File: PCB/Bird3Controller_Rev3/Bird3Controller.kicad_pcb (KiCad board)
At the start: 2 copper layers, 43 x 108 mm, 61 parts, among them IC1 M24C08-RMN6TP, IC2 AP63203WU-7, J1 Bird 3 24-pin Connector, J2 TXW154028S0 Connector, J3 87832-2220, J4 Adafruit USB-C Breakout, Q1 2N7002A, SW1 SW_Boot, SW2 SW_Reset, U1 ESP32-S3-WROOM-1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

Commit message: Switch to thermal reliefs for pad connections except for thermal pads. Also move some traces around to optimize the thermal reliefs
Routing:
- net GND: track 379.3 -> 383.5 mm, vias 145 -> 151

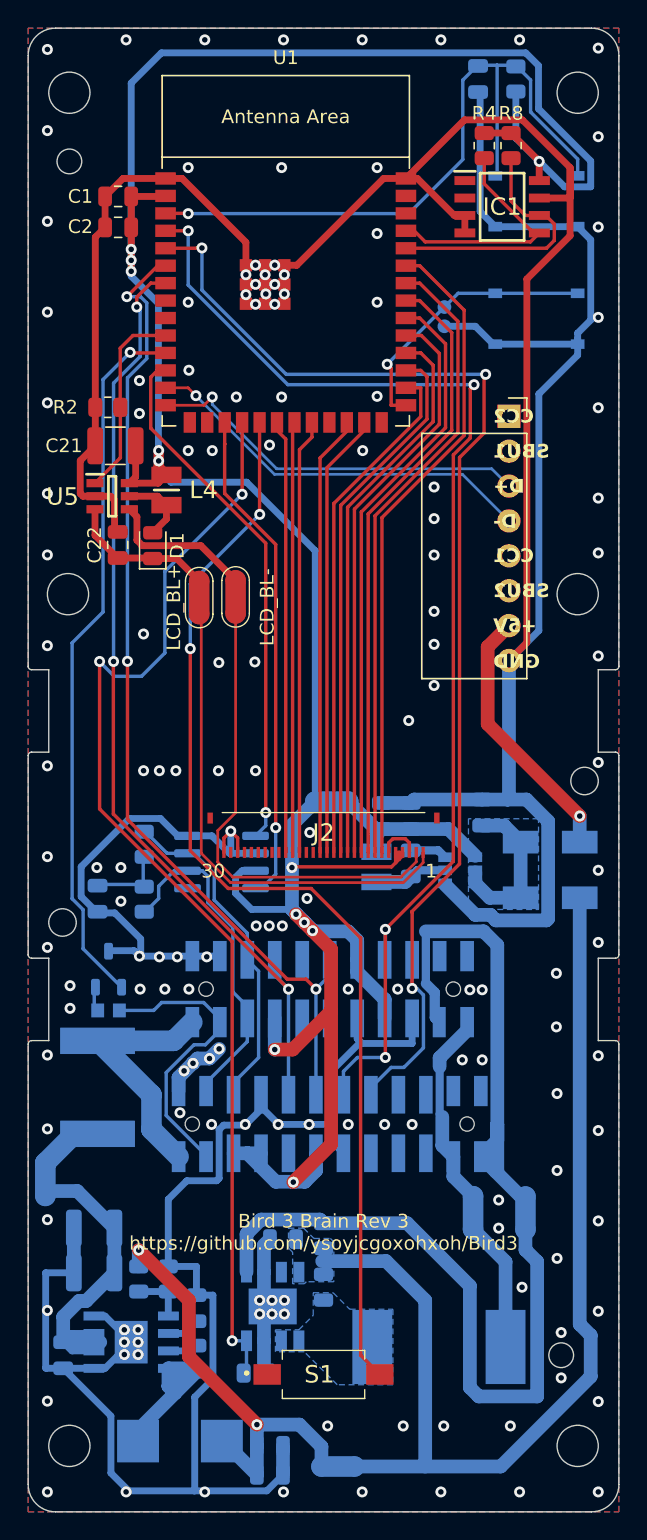
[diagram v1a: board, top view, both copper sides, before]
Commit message: Rearrange and add ground plane vias
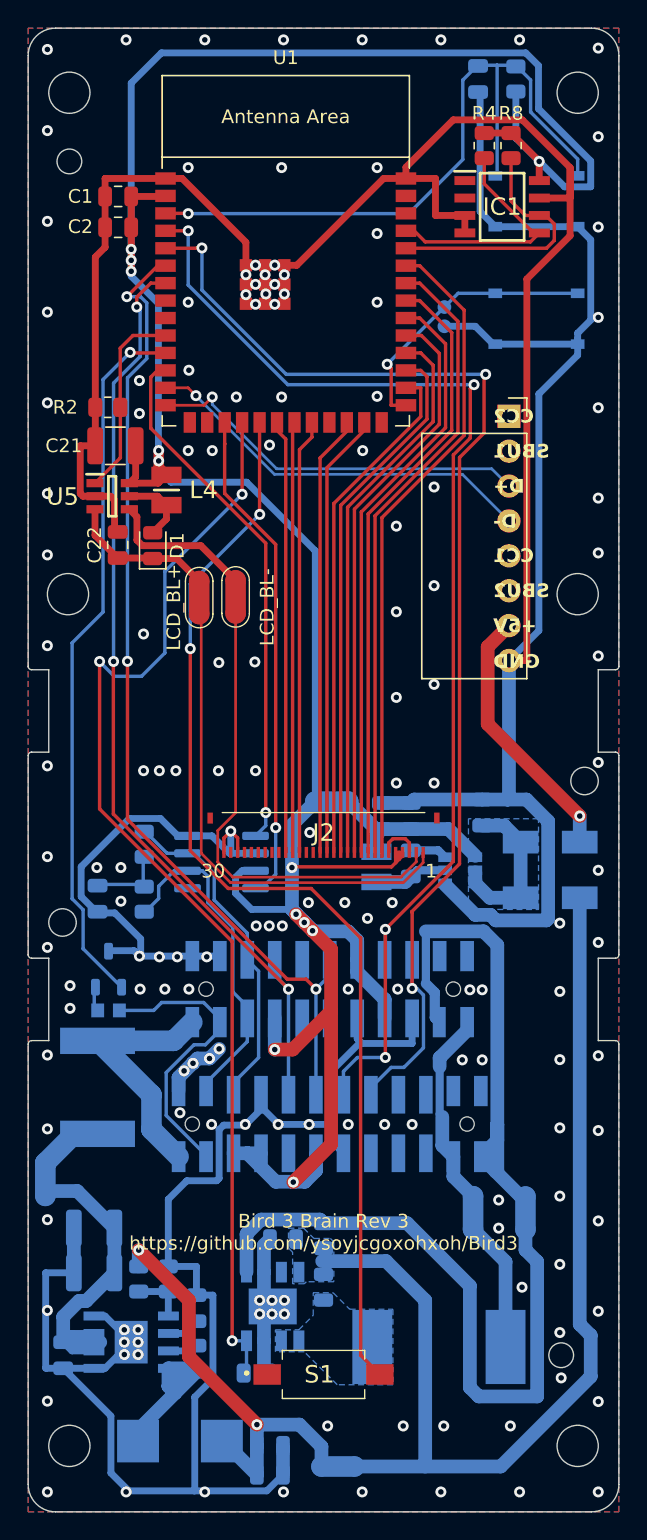
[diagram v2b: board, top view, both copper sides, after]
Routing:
- net GND: track 383.5 -> 387.7 mm, vias 151 -> 156

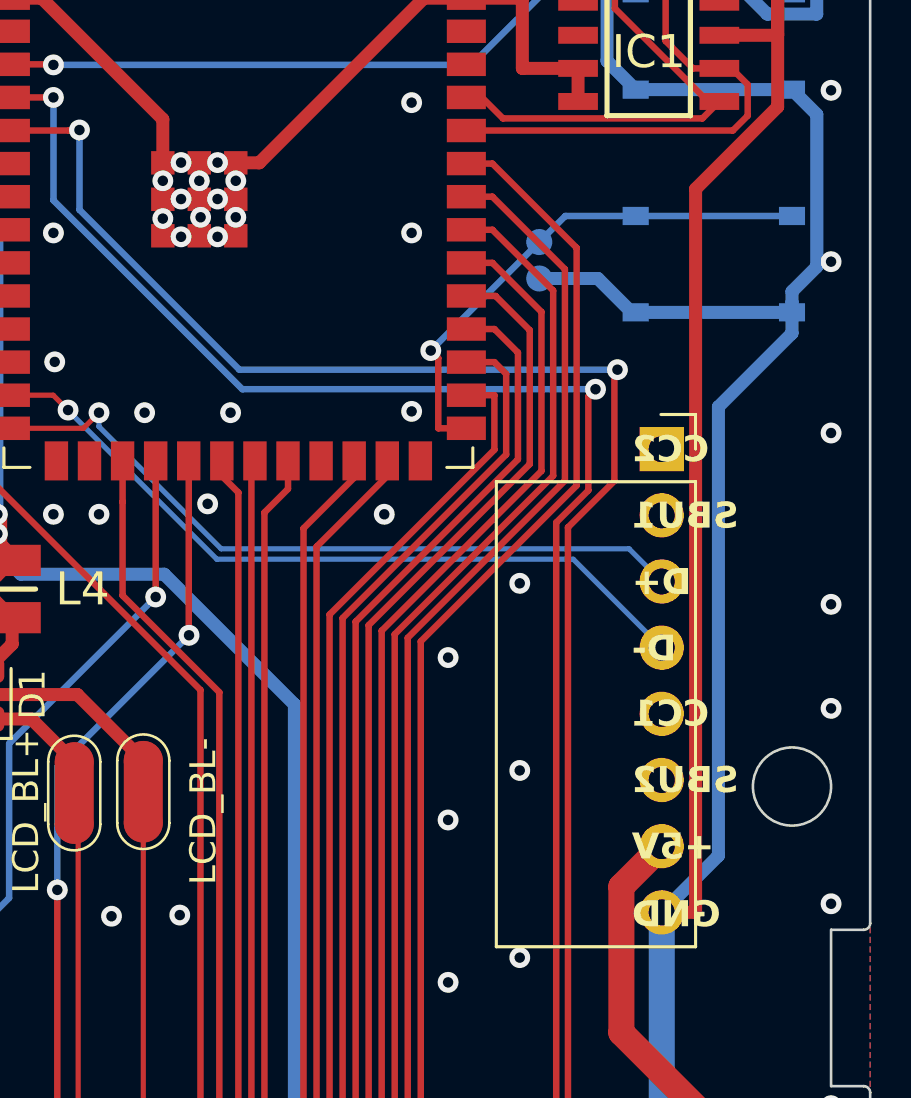
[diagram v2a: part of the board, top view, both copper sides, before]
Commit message: Correct ESP32 thermal pad violations and the USB-C breakout text that keeps moving randomly
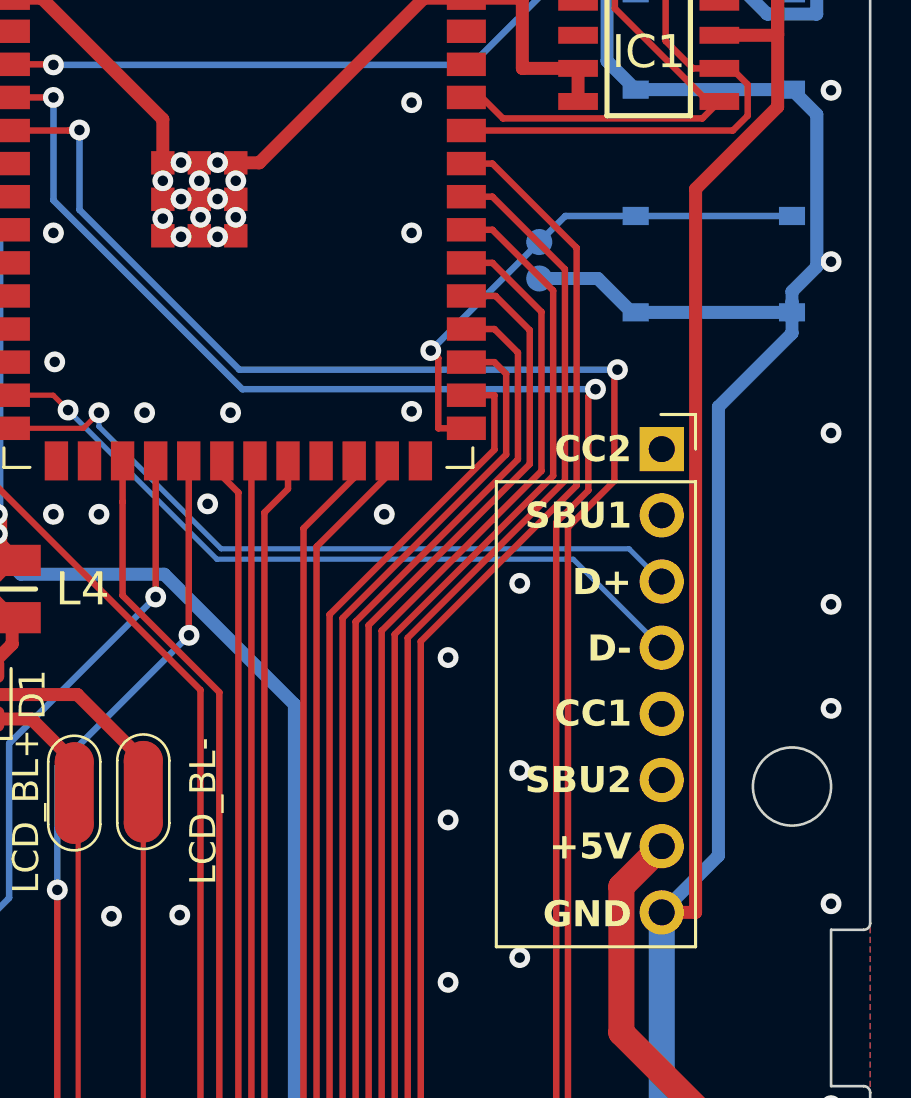
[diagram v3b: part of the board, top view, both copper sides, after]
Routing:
- net GND: track 387.7 -> 396.1 mm
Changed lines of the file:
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@@
 			)
 		)
+		(sheetname "Root")
+		(sheetfile "Bird3Controller.kicad_sch")
 		(attr smd)
 		(fp_line
@@
 			(layer "B.Fab")
 		)
-		(fp_text user "D-"
-			(at 1.15 -7.65 0)
+		(fp_text user "SBU1"
+			(at 1.15 -2.55 0)
 			(unlocked yes)
 			(layer "B.SilkS")
@@
 			)
 		)
-		(fp_text user "CC2"
-			(at 1.15 0 0)
+		(fp_text user "D+"
+			(at 1.15 -5.1 0)
 			(unlocked yes)
 			(layer "B.SilkS")
@@
 			)
 		)
-		(fp_text user "SBU1"
-			(at 1.15 -2.55 0)
+		(fp_text user "+5V"
+			(at 1.15 -15.25 0)
 			(unlocked yes)
 			(layer "B.SilkS")
@@
 			)
 		)
-		(fp_text user "D+"
-			(at 1.15 -5.1 0)
+		(fp_text user "GND"
+			(at 1.15 -17.85 0)
 			(unlocked yes)
 			(layer "B.SilkS")
@@
 			)
 		)
-		(fp_text user "GND"
-			(at 1.15 -17.85 0)
+		(fp_text user "D-"
+			(at 1.15 -7.65 0)
 			(unlocked yes)
 			(layer "B.SilkS")
@@
 			)
 		)
-		(fp_text user "+5V"
-			(at 1.15 -15.25 0)
+		(fp_text user "CC2"
+			(at 1.15 0 0)
 			(unlocked yes)
 			(layer "B.SilkS")
@@
 			)
 		)
-		(fp_text user "CC2"
-			(at 1.15 0 0)
+		(fp_text user "SBU1"
+			(at 1.15 -2.55 0)
 			(unlocked yes)
 			(layer "F.SilkS")
@@
 					(bold yes)
 				)
-				(justify right mirror)
+				(justify right)
 			)
 		)
-		(fp_text user "CC1"
-			(at 1.15 -10.15 0)
+		(fp_text user "D-"
+			(at 1.15 -7.65 0)
 			(unlocked yes)
 			(layer "F.SilkS")
@@
 					(bold yes)
 				)
-				(justify right mirror)
+				(justify right)
 			)
 		)
-		(fp_text user "+5V"
-			(at 1.15 -15.25 0)
+		(fp_text user "SBU2"
+			(at 1.15 -12.7 0)
 			(unlocked yes)
 			(layer "F.SilkS")
@@
 					(bold yes)
 				)
-				(justify right mirror)
+				(justify right)
 			)
 		)
-		(fp_text user "D+"
-			(at 1.15 -5.1 0)
+		(fp_text user "+5V"
+			(at 1.15 -15.25 0)
 			(unlocked yes)
 			(layer "F.SilkS")
@@
 					(bold yes)
 				)
-				(justify right mirror)
+				(justify right)
 			)
 		)
-		(fp_text user "D-"
-			(at 1.15 -7.65 0)
+		(fp_text user "CC2"
+			(at 1.15 0 0)
 			(unlocked yes)
 			(layer "F.SilkS")
@@
 					(bold yes)
 				)
-				(justify right mirror)
+				(justify right)
 			)
 		)
-		(fp_text user "SBU1"
-			(at 1.15 -2.55 0)
+		(fp_text user "GND"
+			(at 1.15 -17.85 0)
 			(unlocked yes)
 			(layer "F.SilkS")
@@
 					(bold yes)
 				)
-				(justify right mirror)
+				(justify right)
 			)
 		)
-		(fp_text user "GND"
-			(at 1.15 -17.85 0)
+		(fp_text user "D+"
+			(at 1.15 -5.1 0)
 			(unlocked yes)
 			(layer "F.SilkS")
@@
 					(bold yes)
 				)
-				(justify right mirror)
+				(justify right)
 			)
 		)
-		(fp_text user "SBU2"
-			(at 1.15 -12.7 0)
+		(fp_text user "CC1"
+			(at 1.15 -10.15 0)
 			(unlocked yes)
 			(layer "F.SilkS")
@@
 					(bold yes)
 				)
-				(justify right mirror)
+				(justify right)
 			)
 		)
@@
 	)
 	(segment
+		(start 179.15 62.06)
+		(end 176.35 62.06)
+		(width 0.5)
+		(layer "F.Cu")
+		(net 5)
+	)
+	(segment
 		(start 174.75 100.95)
 		(end 175.25 100.45)
@@
 	)
 	(segment
+		(start 177.75 62.06)
+		(end 177.75 59.26)
+		(width 0.5)
+		(layer "F.Cu")
+		(net 5)
+	)
+	(segment
 		(start 165.3875 58.6625)
 		(end 166.1 57.95)
@@
 		(layer "F.Cu")
 		(net 5)
+	)
+	(segment
+		(start 179.15 60.66)
+		(end 176.35 60.66)
+		(width 0.5)
+		(layer "F.Cu")
+		(net 5)

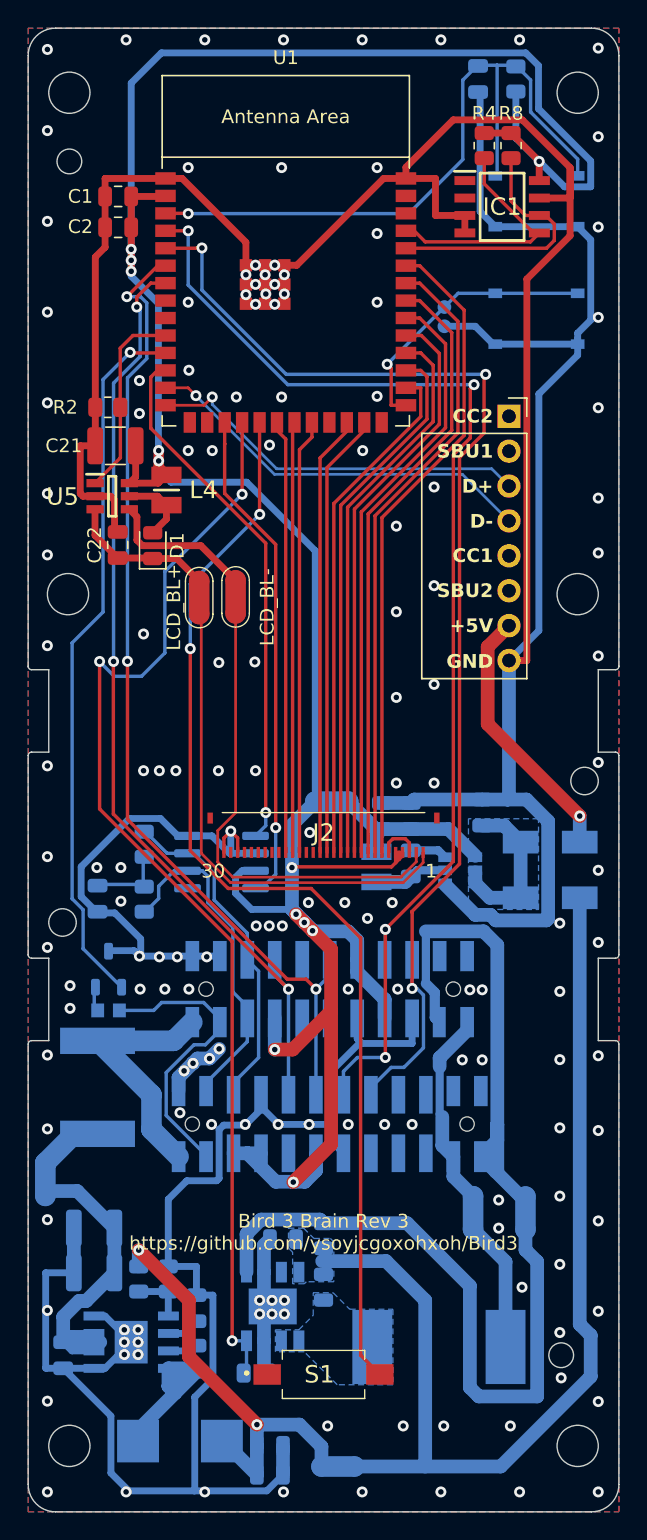
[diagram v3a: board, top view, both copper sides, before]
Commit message: Update footprints to better indicate pin 1
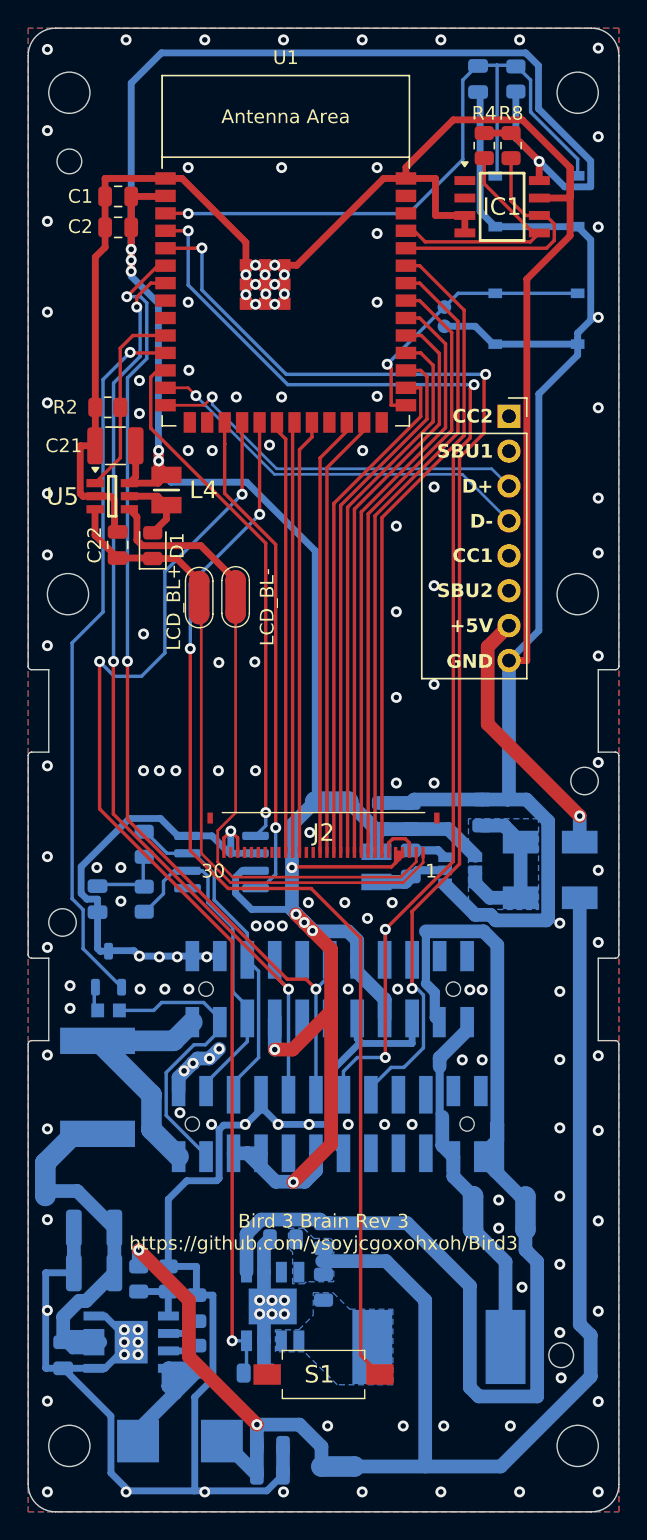
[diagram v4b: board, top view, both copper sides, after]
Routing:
- net GND: track 396.1 -> 394.9 mm

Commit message: Add test points
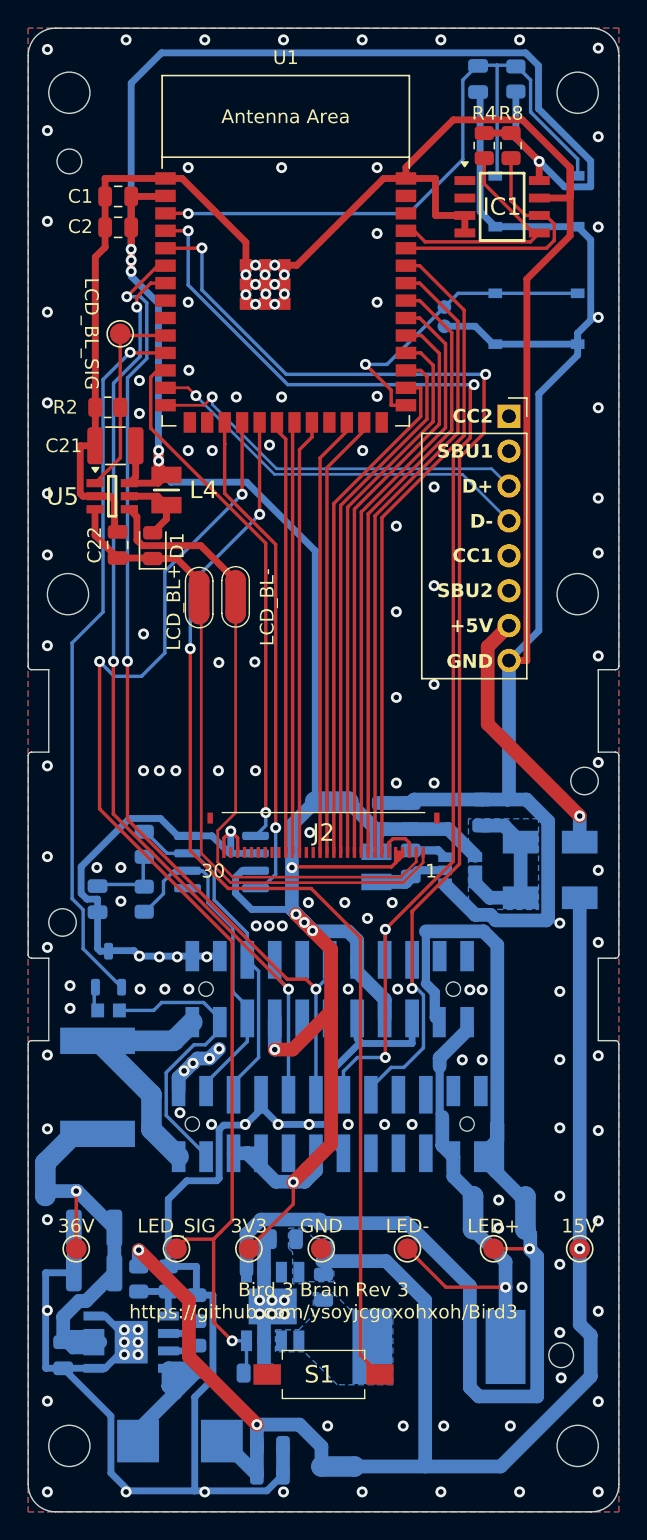
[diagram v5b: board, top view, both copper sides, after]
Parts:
- added TP10: LED+, Bird3Controller:Labeled_TestPoint_1.5mm, F.Cu at (194.4, 130.8)
- added TP11: LED-, Bird3Controller:Labeled_TestPoint_1.5mm, F.Cu at (188.1, 130.8)
- added TP12: 3V3, Bird3Controller:Labeled_TestPoint_1.5mm, F.Cu at (176.6, 130.8)
- added TP13: LED_SIG, Bird3Controller:Labeled_TestPoint_1.5mm, F.Cu at (171.3, 130.8)
- added TP14: LCD_BL_SIG, Bird3Controller:Labeled_TestPoint_1.5mm, F.Cu at (167.2, 64.2)
- added TP15: GND, Bird3Controller:Labeled_TestPoint_1.5mm, F.Cu at (181.8, 130.8)
- added TP8: 36V, Bird3Controller:Labeled_TestPoint_1.5mm, F.Cu at (164.0, 130.8)
- added TP9: 15V, Bird3Controller:Labeled_TestPoint_1.5mm, F.Cu at (200.7, 130.8)
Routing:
- net Net-(L1-Pad2): track 9.55 -> 17.9 mm, vias 0 -> 1
- net +3V3: track 212.7 -> 218.9 mm
- net Net-(U4-EN): track 24.1 -> 28.3 mm, vias 0 -> 1
- net /LED_SIG: track 82.0 -> 86.1 mm
- net Net-(U2-SET): track 46.5 -> 49.2 mm, vias 0 -> 1
- net Net-(U1-GPIO0/Strap): track 20.2 -> 22.4 mm
- net /LCD_BL_SIG: track 14.3 -> 14.8 mm
- net +15V: track 75.9 -> 76.0 mm, vias 0 -> 1
